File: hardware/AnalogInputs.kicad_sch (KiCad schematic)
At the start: 46 parts, among them U2 MCP6N11-005, U3 MCP6N11-005, U4 MCP6001, U5 MCP6001

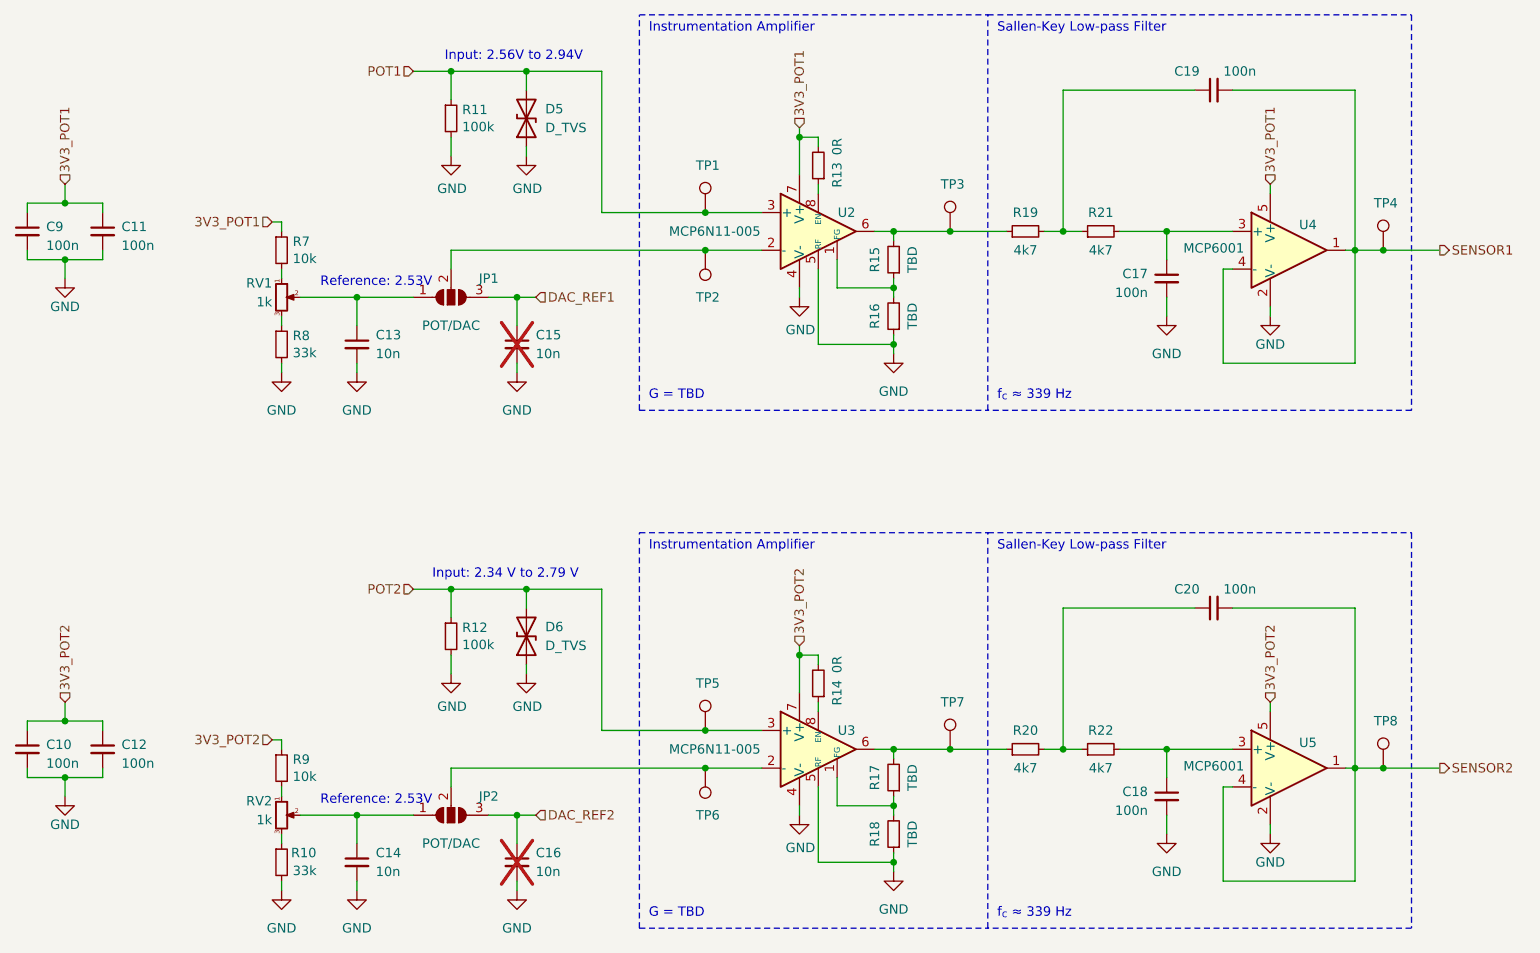
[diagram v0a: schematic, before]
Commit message: Add brake pressure sensors
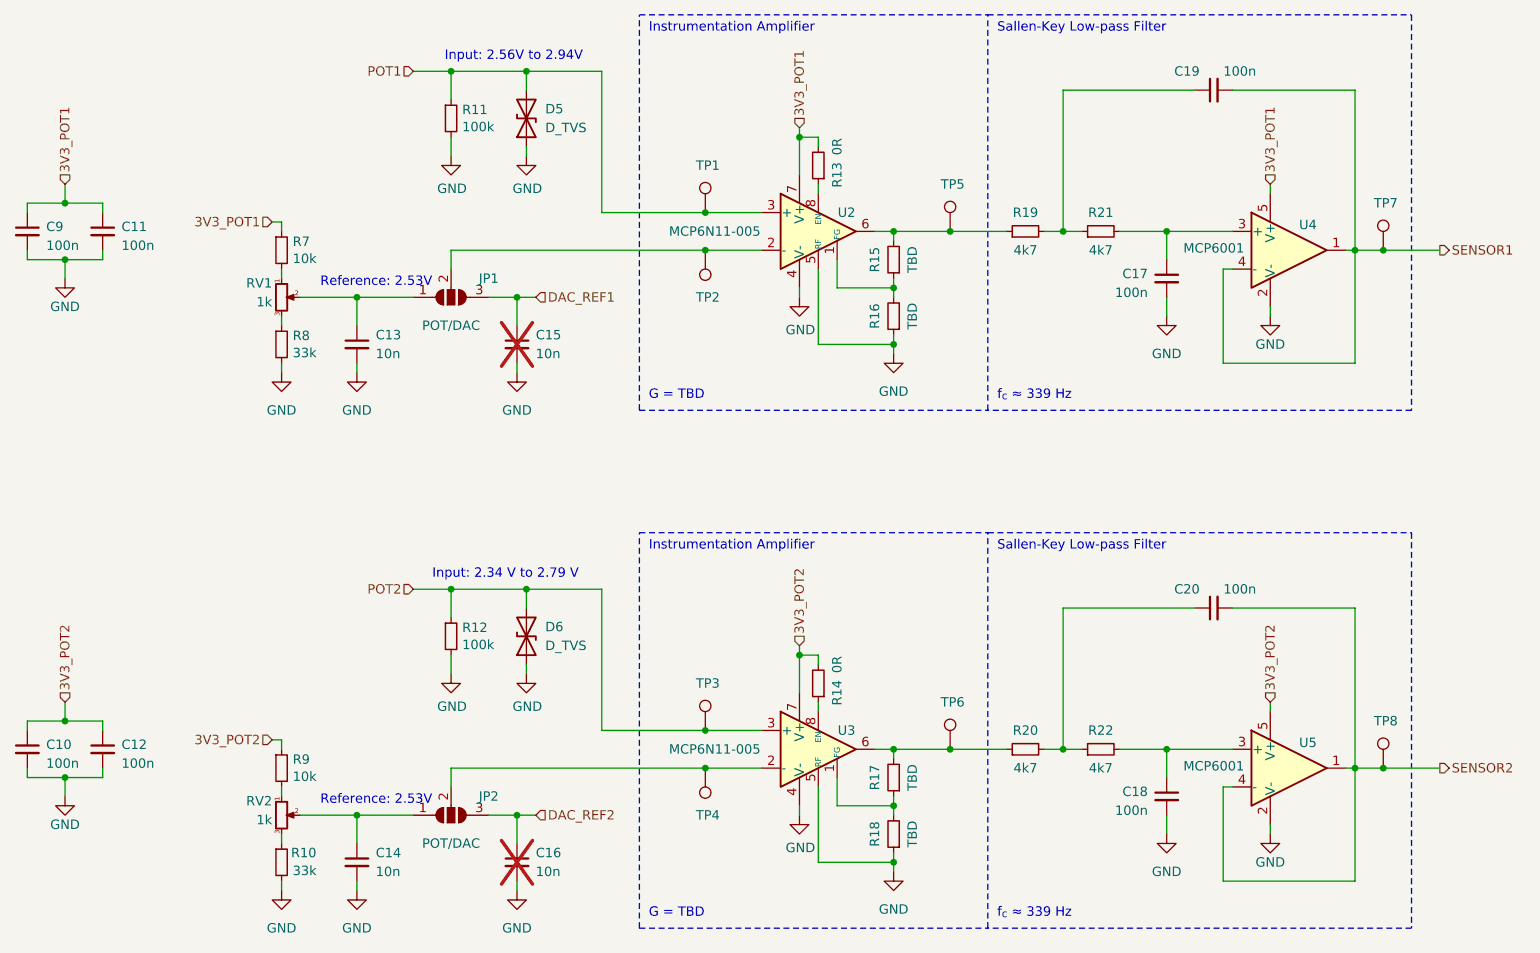
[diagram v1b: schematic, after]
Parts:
- renumbered TP5 to TP3, TP6 to TP4, TP3 to TP5, TP7 to TP6, TP4 to TP7
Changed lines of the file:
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@@
   (symbol (lib_id "Connector:TestPoint") (at 181.61 59.69 0) (unit 1)
     (in_bom yes) (on_board yes) (dnp no)
-    (property "Reference" "TP3" (at 180.34 53.34 0)
+    (property "Reference" "TP5" (at 180.34 53.34 0)
       (effects (font (size 1.27 1.27)) (justify left))
     )
@@
       (project "APPS"
         (path "/fc4ad874-c922-4070-89f9-7262080469d8/00000000-0000-0000-0000-00006068dc5c"
-          (reference "TP3") (unit 1)
+          (reference "TP5") (unit 1)
         )
       )
@@
   (symbol (lib_id "Connector:TestPoint") (at 240.03 62.23 0) (unit 1)
     (in_bom yes) (on_board yes) (dnp no)
-    (property "Reference" "TP4" (at 238.76 55.88 0)
+    (property "Reference" "TP7" (at 238.76 55.88 0)
       (effects (font (size 1.27 1.27)) (justify left))
     )
@@
       (project "APPS"
         (path "/fc4ad874-c922-4070-89f9-7262080469d8/00000000-0000-0000-0000-00006068dc5c"
-          (reference "TP4") (unit 1)
+          (reference "TP7") (unit 1)
         )
       )
@@
   (symbol (lib_id "Connector:TestPoint") (at 181.61 129.54 0) (unit 1)
     (in_bom yes) (on_board yes) (dnp no)
-    (property "Reference" "TP7" (at 180.34 123.19 0)
+    (property "Reference" "TP6" (at 180.34 123.19 0)
       (effects (font (size 1.27 1.27)) (justify left))
     )
@@
       (project "APPS"
         (path "/fc4ad874-c922-4070-89f9-7262080469d8/00000000-0000-0000-0000-00006068dc5c"
-          (reference "TP7") (unit 1)
+          (reference "TP6") (unit 1)
         )
       )
@@
   (symbol (lib_id "Connector:TestPoint") (at 148.59 132.08 180) (unit 1)
     (in_bom yes) (on_board yes) (dnp no)
-    (property "Reference" "TP6" (at 147.32 138.43 0)
+    (property "Reference" "TP4" (at 147.32 138.43 0)
       (effects (font (size 1.27 1.27)) (justify right))
     )
@@
       (project "APPS"
         (path "/fc4ad874-c922-4070-89f9-7262080469d8/00000000-0000-0000-0000-00006068dc5c"
-          (reference "TP6") (unit 1)
+          (reference "TP4") (unit 1)
         )
       )
@@
   (symbol (lib_id "Connector:TestPoint") (at 148.59 127 0) (unit 1)
     (in_bom yes) (on_board yes) (dnp no)
-    (property "Reference" "TP5" (at 147.32 120.65 0)
+    (property "Reference" "TP3" (at 147.32 120.65 0)
       (effects (font (size 1.27 1.27)) (justify left))
     )
@@
       (project "APPS"
         (path "/fc4ad874-c922-4070-89f9-7262080469d8/00000000-0000-0000-0000-00006068dc5c"
-          (reference "TP5") (unit 1)
-        )
-      )
+          (reference "TP3") (unit 1)
+        )
+      )

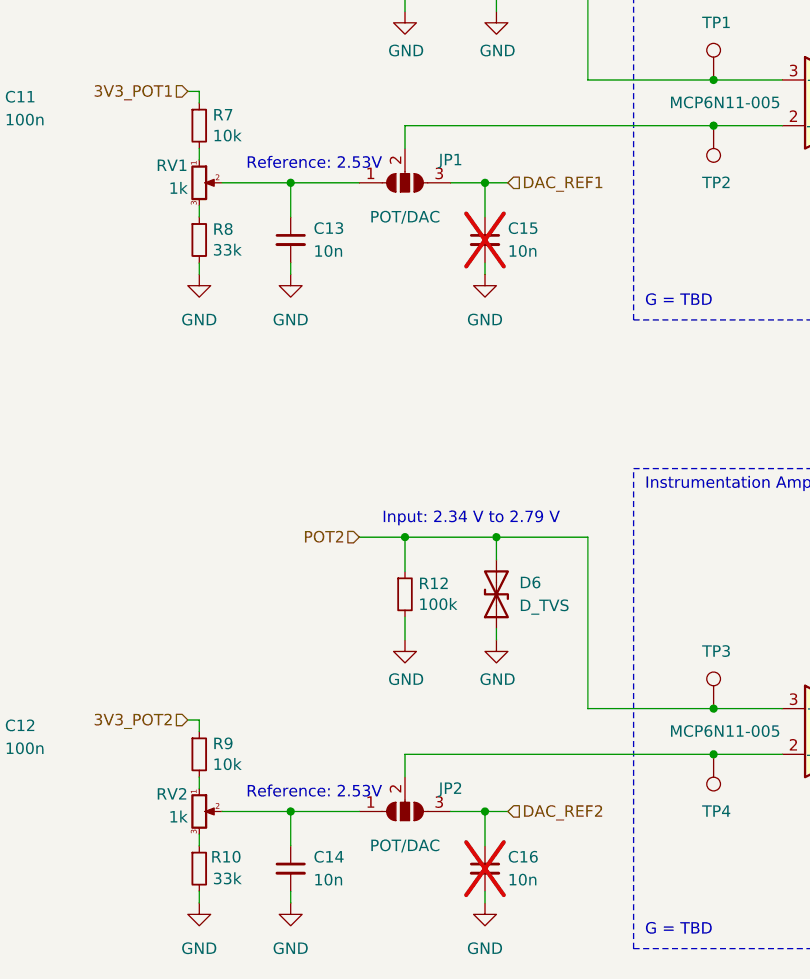
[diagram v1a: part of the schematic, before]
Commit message: Use bridged solder jumpers
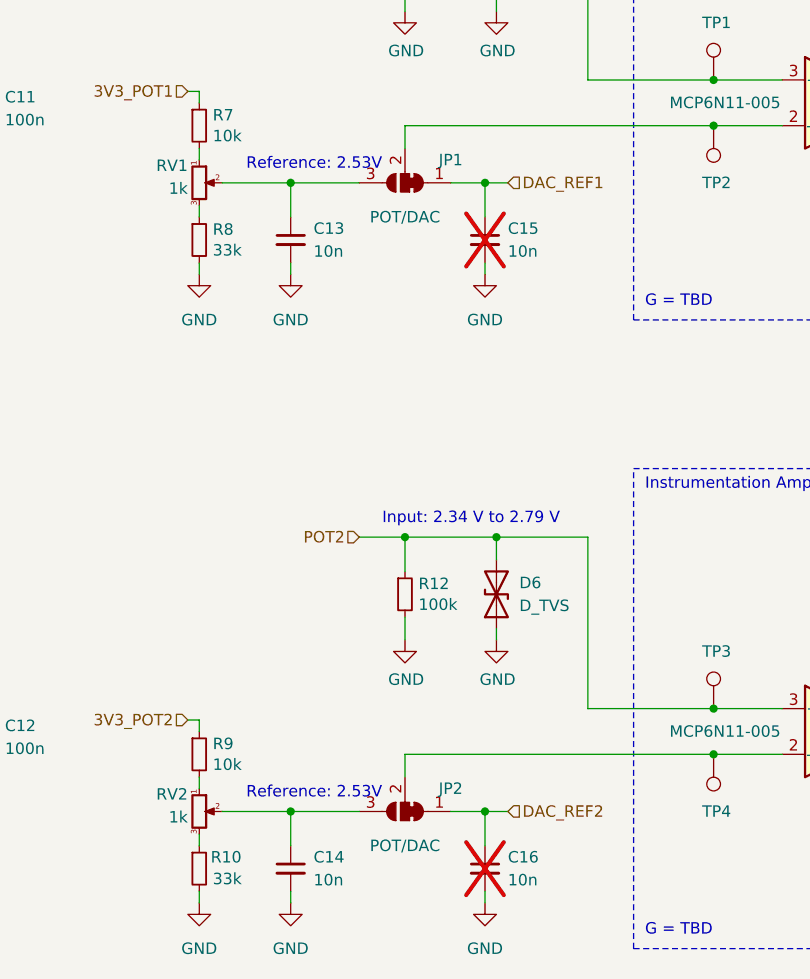
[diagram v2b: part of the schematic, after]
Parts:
- JP1, JP2: footprint Jumper:SolderJumper-3_P1.3mm_Open_RoundedPad1.0x1.5mm_NumberLabels -> Jumper:SolderJumper-3_P1.3mm_Bridged12_RoundedPad1.0x1.5mm; symbol Jumper:SolderJumper_3_Open -> Jumper:SolderJumper_3_Bridged12
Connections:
- net DAC_REF1: now also JP1.1 (A); no longer JP1.3 (B)
- net DAC_REF2: now also JP2.1 (A); no longer JP2.3 (B)
- net at C13.1, RV1.2: now also JP1.3 (B); no longer JP1.1 (A)
- net at C14.1, RV2.2: now also JP2.3 (B); no longer JP2.1 (A)
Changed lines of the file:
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@@
     )
   )
-  (symbol (lib_id "Jumper:SolderJumper_3_Open") (at 114.3 138.43 0) (mirror x) (unit 1)
+  (symbol (lib_id "Jumper:SolderJumper_3_Bridged12") (at 114.3 138.43 180) (unit 1)
     (in_bom yes) (on_board yes) (dnp no)
     (property "Reference" "JP2" (at 119.38 135.89 0)
@@
       (effects (font (size 1.27 1.27)))
     )
-    (property "Footprint" "Jumper:SolderJumper-3_P1.3mm_Open_RoundedPad1.0x1.5mm_NumberLabels" (at 114.3 138.43 0)
+    (property "Footprint" "Jumper:SolderJumper-3_P1.3mm_Bridged12_RoundedPad1.0x1.5mm" (at 114.3 138.43 0)
       (effects (font (size 1.27 1.27)) hide)
     )
@@
     )
   )
-  (symbol (lib_id "Jumper:SolderJumper_3_Open") (at 114.3 68.58 0) (mirror x) (unit 1)
+  (symbol (lib_id "Jumper:SolderJumper_3_Bridged12") (at 114.3 68.58 180) (unit 1)
     (in_bom yes) (on_board yes) (dnp no)
     (property "Reference" "JP1" (at 119.38 66.04 0)
@@
       (effects (font (size 1.27 1.27)))
     )
-    (property "Footprint" "Jumper:SolderJumper-3_P1.3mm_Open_RoundedPad1.0x1.5mm_NumberLabels" (at 114.3 68.58 0)
+    (property "Footprint" "Jumper:SolderJumper-3_P1.3mm_Bridged12_RoundedPad1.0x1.5mm" (at 114.3 68.58 0)
       (effects (font (size 1.27 1.27)) hide)
     )

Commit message: Change test points footprints
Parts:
- TP1: value P1 -> APPS_P; footprint TestPoint:TestPoint_Pad_1.0x1.0mm -> TestPoint:TestPoint_Pad_D1.0mm
- TP2: value N1 -> APPS_N; footprint TestPoint:TestPoint_Pad_1.0x1.0mm -> TestPoint:TestPoint_Pad_D1.0mm
- TP3: value P2 -> APPS_P; footprint TestPoint:TestPoint_Pad_1.0x1.0mm -> TestPoint:TestPoint_Pad_D1.0mm
- TP4: value N2 -> APPS_N; footprint TestPoint:TestPoint_Pad_1.0x1.0mm -> TestPoint:TestPoint_Pad_D1.0mm
- TP5: value O1 -> APPS_MID; footprint TestPoint:TestPoint_Pad_1.0x1.0mm -> TestPoint:TestPoint_Pad_D1.0mm
- TP6: value O2 -> APPS_MID; footprint TestPoint:TestPoint_Pad_1.0x1.0mm -> TestPoint:TestPoint_Pad_D1.0mm
- TP7: value F1 -> APPS_OUT; footprint TestPoint:TestPoint_Pad_1.0x1.0mm -> TestPoint:TestPoint_Pad_D1.0mm
- TP8: value F2 -> APPS_OUT; footprint TestPoint:TestPoint_Pad_1.0x1.0mm -> TestPoint:TestPoint_Pad_D1.0mm
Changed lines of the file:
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@@
       (effects (font (size 1.27 1.27)) (justify left))
     )
-    (property "Value" "O1" (at 184.15 58.293 0)
+    (property "Value" "APPS_MID" (at 184.15 58.293 0)
       (effects (font (size 1.27 1.27)) (justify left) hide)
     )
-    (property "Footprint" "TestPoint:TestPoint_Pad_1.0x1.0mm" (at 186.69 59.69 0)
+    (property "Footprint" "TestPoint:TestPoint_Pad_D1.0mm" (at 186.69 59.69 0)
       (effects (font (size 1.27 1.27)) hide)
     )
@@
       (effects (font (size 1.27 1.27)) (justify right))
     )
-    (property "Value" "N1" (at 151.13 67.437 0)
+    (property "Value" "APPS_N" (at 151.13 67.437 0)
       (effects (font (size 1.27 1.27)) (justify right) hide)
     )
-    (property "Footprint" "TestPoint:TestPoint_Pad_1.0x1.0mm" (at 143.51 62.23 0)
+    (property "Footprint" "TestPoint:TestPoint_Pad_D1.0mm" (at 143.51 62.23 0)
       (effects (font (size 1.27 1.27)) hide)
     )
@@
       (effects (font (size 1.27 1.27)) (justify left))
     )
-    (property "Value" "F2" (at 242.57 130.683 0)
+    (property "Value" "APPS_OUT" (at 242.57 130.683 0)
       (effects (font (size 1.27 1.27)) (justify left) hide)
     )
-    (property "Footprint" "TestPoint:TestPoint_Pad_1.0x1.0mm" (at 245.11 132.08 0)
+    (property "Footprint" "TestPoint:TestPoint_Pad_D1.0mm" (at 245.11 132.08 0)
       (effects (font (size 1.27 1.27)) hide)
     )
@@
       (effects (font (size 1.27 1.27)) (justify left))
     )
-    (property "Value" "F1" (at 242.57 60.833 0)
+    (property "Value" "APPS_OUT" (at 242.57 60.833 0)
       (effects (font (size 1.27 1.27)) (justify left) hide)
     )
-    (property "Footprint" "TestPoint:TestPoint_Pad_1.0x1.0mm" (at 245.11 62.23 0)
+    (property "Footprint" "TestPoint:TestPoint_Pad_D1.0mm" (at 245.11 62.23 0)
       (effects (font (size 1.27 1.27)) hide)
     )
@@
       (effects (font (size 1.27 1.27)) (justify left))
     )
-    (property "Value" "O2" (at 184.15 128.143 0)
+    (property "Value" "APPS_MID" (at 184.15 128.143 0)
       (effects (font (size 1.27 1.27)) (justify left) hide)
     )
-    (property "Footprint" "TestPoint:TestPoint_Pad_1.0x1.0mm" (at 186.69 129.54 0)
+    (property "Footprint" "TestPoint:TestPoint_Pad_D1.0mm" (at 186.69 129.54 0)
       (effects (font (size 1.27 1.27)) hide)
     )
@@
       (effects (font (size 1.27 1.27)) (justify left))
     )
-    (property "Value" "P1" (at 151.13 55.753 0)
+    (property "Value" "APPS_P" (at 151.13 55.753 0)
       (effects (font (size 1.27 1.27)) (justify left) hide)
     )
-    (property "Footprint" "TestPoint:TestPoint_Pad_1.0x1.0mm" (at 153.67 57.15 0)
+    (property "Footprint" "TestPoint:TestPoint_Pad_D1.0mm" (at 153.67 57.15 0)
       (effects (font (size 1.27 1.27)) hide)
     )
@@
       (effects (font (size 1.27 1.27)) (justify right))
     )
-    (property "Value" "N2" (at 151.13 137.287 0)
+    (property "Value" "APPS_N" (at 151.13 137.287 0)
       (effects (font (size 1.27 1.27)) (justify right) hide)
     )
-    (property "Footprint" "TestPoint:TestPoint_Pad_1.0x1.0mm" (at 143.51 132.08 0)
+    (property "Footprint" "TestPoint:TestPoint_Pad_D1.0mm" (at 143.51 132.08 0)
       (effects (font (size 1.27 1.27)) hide)
     )
@@
       (effects (font (size 1.27 1.27)) (justify left))
     )
-    (property "Value" "P2" (at 151.13 125.603 0)
+    (property "Value" "APPS_P" (at 151.13 125.603 0)
       (effects (font (size 1.27 1.27)) (justify left) hide)
     )
-    (property "Footprint" "TestPoint:TestPoint_Pad_1.0x1.0mm" (at 153.67 127 0)
-      (effects (font (size 1.27 1.27)) hide)
-    )
+    (property "Footprint" "TestPoint:TestPoint_Pad_D1.0mm" (at 153.67 127 0)
+      (effects (font (size 1.27 1.27)) hide)
+    )
